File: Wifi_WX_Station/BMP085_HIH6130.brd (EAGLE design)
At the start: 20.9 x 20.6 mm, 8 parts, among them U1 HIH_6130

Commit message: updated BOM with all prices- As Checked in to BATCH PCB
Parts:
- removed JP1: (no value), Headers:1X06
- added JP2: (no value), wifi_WX:1X05
- moved C3 0.63 mm to (11.4, 14.6)
- moved R2 0.63 mm to (18.4, 14.0)
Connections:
- net +3V3: now also JP2.5; no longer JP1.6
- net GND: now also JP2.1; no longer JP1.1
- net SCL: now also JP2.4; no longer JP1.4
- net SDA: now also JP2.3; no longer JP1.3
- net XCLR: now also JP2.2; no longer JP1.2
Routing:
- net +3V3: track 38.4 -> 43.3 mm
- net GND: track 49.3 -> 46.5 mm, vias 0 -> 1
- net SCL: track 16.7 -> 18.0 mm
- net XCLR: track 12.6 -> 13.5 mm
- net SDA: track 20.9 -> 20.3 mm
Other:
- board size 20.9 x 20.6 mm -> 21.6 x 20.6 mm

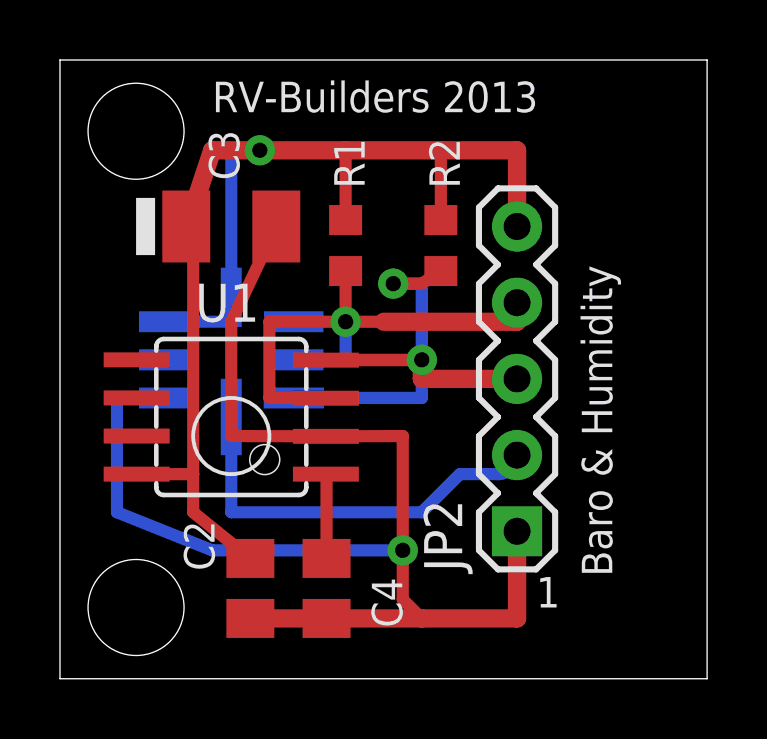
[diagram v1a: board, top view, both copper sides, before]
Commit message: added SILabs Hygrometer board Added frames to the schematics
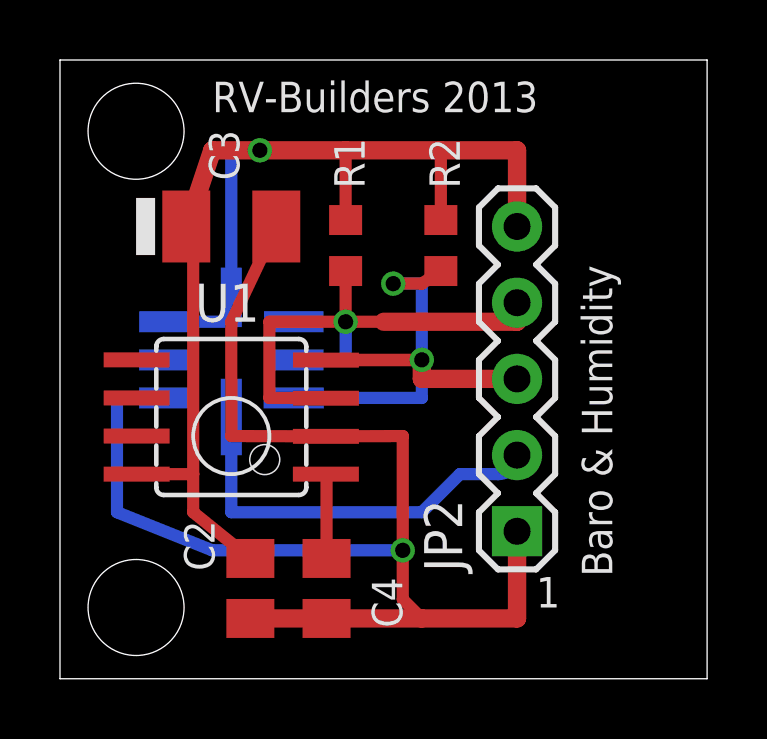
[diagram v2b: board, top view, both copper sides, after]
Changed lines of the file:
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@@
 </class>
 </classes>
-<designrules name="sparkfun">
-<description language="en">&lt;b&gt;SPARKFUN Design Rules&lt;/b&gt;
+<designrules name="Elecrow_2-layer_with reduced cream mask">
+<description language="de">&lt;b&gt;EAGLE Design Rules&lt;/b&gt;
 &lt;p&gt;
-The Sparkfun Design Rules have been set to cover
-a wide range of applications. Your particular design
-may have different requirements, so please make the
-necessary adjustments and save your customized
-design rules under a new name.</description>
+Die Standard-Design-Rules sind so gewählt, dass sie für
+die meisten Anwendungen passen. Sollte ihre Platine
+besondere Anforderungen haben, treffen Sie die erforderlichen
+Einstellungen hier und speichern die Design Rules unter
+einem neuen Namen ab.</description>
+<description language="en">&lt;b&gt;ELCROW rules&lt;/b&gt;
+</description>
+<description language="zh">&lt;b&gt;Elecrow EAGLE Design Rules&lt;/b&gt;
+</description>
 <param name="layerSetup" value="(1*16)"/>
 <param name="mtCopper" value="0.035mm 0.035mm 0.035mm 0.035mm 0.035mm 0.035mm 0.035mm 0.035mm 0.035mm 0.035mm 0.035mm 0.035mm 0.035mm 0.035mm 0.035mm 0.035mm"/>
 <param name="mtIsolate" value="1.5mm 0.15mm 0.2mm 0.15mm 0.2mm 0.15mm 0.2mm 0.15mm 0.2mm 0.15mm 0.2mm 0.15mm 0.2mm 0.15mm 0.2mm"/>
-<param name="mdWireWire" value="8mil"/>
-<param name="mdWirePad" value="8mil"/>
-<param name="mdWireVia" value="8mil"/>
-<param name="mdPadPad" value="8mil"/>
-<param name="mdPadVia" value="8mil"/>
-<param name="mdViaVia" value="8mil"/>
-<param name="mdSmdPad" value="8mil"/>
-<param name="mdSmdVia" value="8mil"/>
-<param name="mdSmdSmd" value="8mil"/>
+<param name="mdWireWire" value="6mil"/>
+<param name="mdWirePad" value="6mil"/>
+<param name="mdWireVia" value="6mil"/>
+<param name="mdPadPad" value="6mil"/>
+<param name="mdPadVia" value="6mil"/>
+<param name="mdViaVia" value="6mil"/>
+<param name="mdSmdPad" value="0mil"/>
+<param name="mdSmdVia" value="0mil"/>
+<param name="mdSmdSmd" value="0mil"/>
 <param name="mdViaViaSameLayer" value="8mil"/>
 <param name="mnLayersViaInSmd" value="2"/>
 <param name="mdCopperDimension" value="10mil"/>
-<param name="mdDrill" value="8mil"/>
+<param name="mdDrill" value="10mil"/>
 <param name="mdSmdStop" value="0mil"/>
-<param name="msWidth" value="8mil"/>
-<param name="msDrill" value="20mil"/>
-<param name="msMicroVia" value="9.99mm"/>
+<param name="msWidth" value="6mil"/>
+<param name="msDrill" value="12mil"/>
+<param name="msMicroVia" value="12mil"/>
 <param name="msBlindViaRatio" value="0.5"/>
 <param name="rvPadTop" value="0.25"/>
@@
 <param name="rvMicroViaOuter" value="0.25"/>
 <param name="rvMicroViaInner" value="0.25"/>
-<param name="rlMinPadTop" value="12mil"/>
+<param name="rlMinPadTop" value="10mil"/>
 <param name="rlMaxPadTop" value="20mil"/>
 <param name="rlMinPadInner" value="10mil"/>
 <param name="rlMaxPadInner" value="20mil"/>
-<param name="rlMinPadBottom" value="12mil"/>
+<param name="rlMinPadBottom" value="10mil"/>
 <param name="rlMaxPadBottom" value="20mil"/>
-<param name="rlMinViaOuter" value="10mil"/>
+<param name="rlMinViaOuter" value="6mil"/>
 <param name="rlMaxViaOuter" value="20mil"/>
-<param name="rlMinViaInner" value="10mil"/>
+<param name="rlMinViaInner" value="6mil"/>
 <param name="rlMaxViaInner" value="20mil"/>
 <param name="rlMinMicroViaOuter" value="4mil"/>
@@
 <param name="psTop" value="-1"/>
 <param name="psBottom" value="-1"/>
-<param name="psFirst" value="-1"/>
+<param name="psFirst" value="0"/>
 <param name="psElongationLong" value="100"/>
 <param name="psElongationOffset" value="100"/>
 <param name="mvStopFrame" value="1"/>
-<param name="mvCreamFrame" value="0"/>
-<param name="mlMinStopFrame" value="4mil"/>
-<param name="mlMaxStopFrame" value="4mil"/>
-<param name="mlMinCreamFrame" value="0mil"/>
-<param name="mlMaxCreamFrame" value="0mil"/>
-<param name="mlViaStopLimit" value="25mil"/>
+<param name="mvCreamFrame" value="1"/>
+<param name="mlMinStopFrame" value="2mil"/>
+<param name="mlMaxStopFrame" value="2mil"/>
+<param name="mlMinCreamFrame" value="2mil"/>
+<param name="mlMaxCreamFrame" value="2mil"/>
+<param name="mlViaStopLimit" value="100mil"/>
 <param name="srRoundness" value="0"/>
 <param name="srMinRoundness" value="0mil"/>
@@
 <param name="checkAngle" value="0"/>
 <param name="checkFont" value="1"/>
-<param name="checkRestrict" value="1"/>
+<param name="checkRestrict" value="0"/>
 <param name="useDiameter" value="13"/>
 <param name="maxErrors" value="50"/>
